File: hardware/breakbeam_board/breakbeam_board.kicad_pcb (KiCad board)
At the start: 2 copper layers, 25.4 x 19 mm, 6 parts, among them J1 CONN, U1 OPB360N51

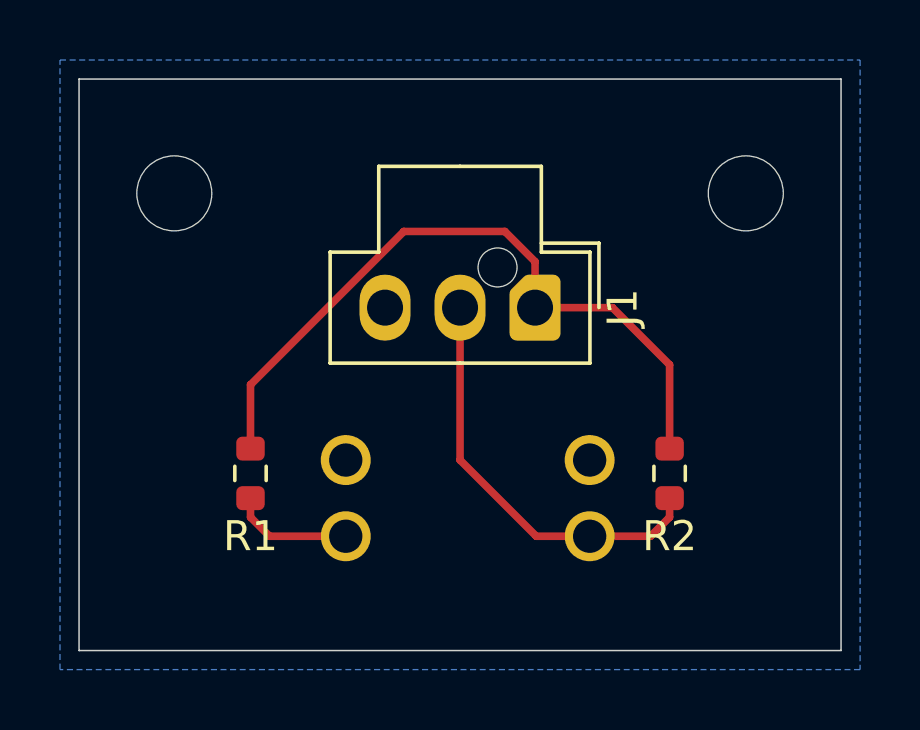
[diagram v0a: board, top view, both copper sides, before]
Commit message: fix layout, add mimi and clean up silkscreen
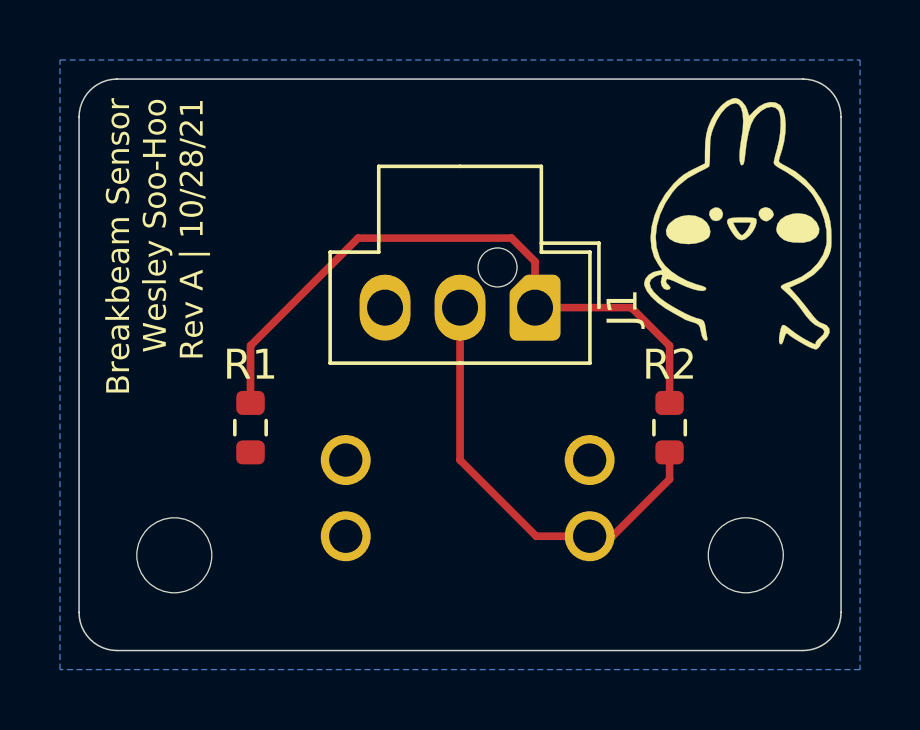
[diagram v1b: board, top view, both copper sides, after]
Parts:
- removed the REF** at (169.5, 84.5)
- removed the REF** at (150.5, 84.5)
- added G***: LOGO, img:mimi, F.Cu at (169.7, 84.8)
- added REF**: MountingHole_2.5mm, MountingHole:MountingHole_2.5mm, F.Cu at (169.5, 96.5)
- added REF**: MountingHole_2.5mm, MountingHole:MountingHole_2.5mm, F.Cu at (150.5, 96.5)
- moved R1 1.53 mm to (153.0, 92.3)
- moved R2 1.53 mm to (167.0, 92.3)
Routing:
- net Net-(R1-Pad2): track 4.07 -> 0.00 mm
- net VCC: track 23.8 -> 21.7 mm
- net /SIG: track 14.0 -> 14.8 mm
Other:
- board size 25.4 x 19 mm -> 25.4 x 19.1 mm
- board text added: "Breakbeam Sensor Wesley Soo-Hoo Rev A | 10/28/21"
- board text added: "GND"
- board text added: "SIG"
- board text added: "VCC"

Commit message: fix missing trace
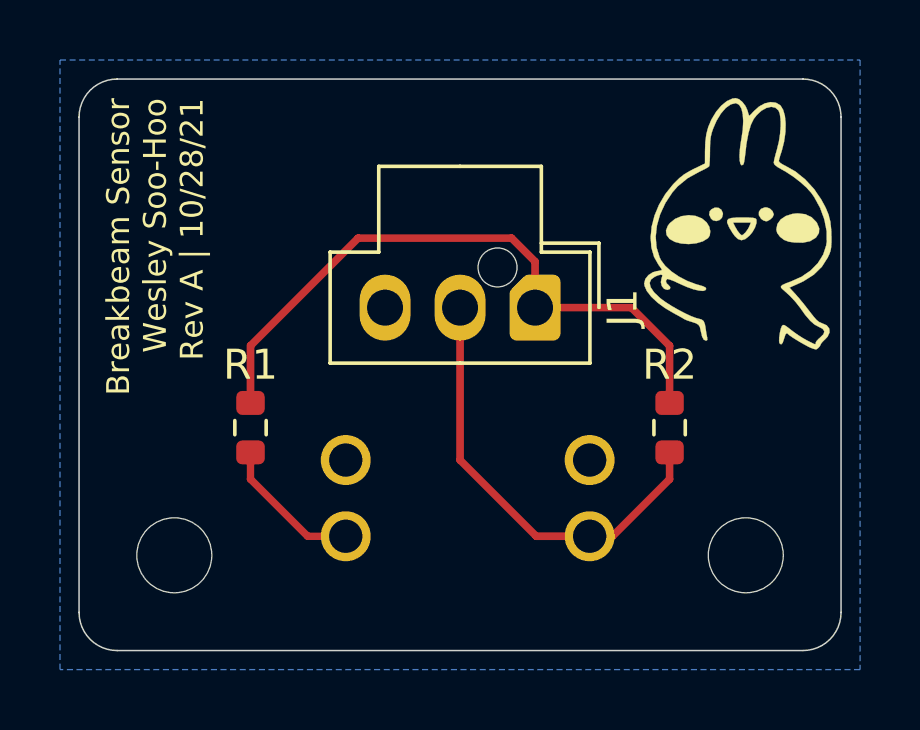
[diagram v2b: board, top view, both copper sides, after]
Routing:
- net Net-(R1-Pad2): track 0.00 -> 4.85 mm
